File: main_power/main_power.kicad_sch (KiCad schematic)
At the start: 11 parts

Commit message: sync
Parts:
- RV?: value ADDVOLATAGE -> xxxV
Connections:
- net 330DC: now reaches C?.1, C?.1, C?.1, C?.1, D?.3 (+)
- net GND: now reaches C?.2, C?.2, C?.2, C?.2, D?.1 (-)
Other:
- added sheet pico_gate_driver (pico_gate_driver.kicad_sch)
- note added: "230 AC to 330 DC"
- note added: "Amount of capacitors and thier capacity have to be selected manually based on measurements/furnace behaviour and thermal wire resistance."
- note removed: "Amount of capacitors and thier capacity have to be selected manually based on measurements and thermal wire resistance."
- moved on the sheet: C?, D?, F?, P?, RV?

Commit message: repo cleaning
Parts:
- added TP?: BINDIN_POST, symbol Connector:TestPoint
- added TP?: BINDING_POST, symbol Connector:TestPoint
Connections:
- net GND renamed GND1
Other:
- added sheet PICO (pico.kicad_sch)
- added sheet converter (converter.kicad_sch)
- note added: "230 AC to 320 DC"
- note removed: "230 AC to 330 DC"
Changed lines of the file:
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@@
 		)
 	)
-	(text "230 AC to 330 DC"
+	(text "230 AC to 320 DC"
 		(exclude_from_sim no)
 		(at 100.838 17.78 0)
@@
 	)
 	(symbol
+		(lib_id "Connector:TestPoint")
+		(at 198.12 52.07 180)
+		(unit 1)
+		(exclude_from_sim no)
+		(in_bom yes)
+		(on_board yes)
+		(dnp no)
+		(fields_autoplaced yes)
+		(property "Reference" "TP?"
+			(at 200.66 54.1019 0)
+			(effects
+				(font
+					(size 1.27 1.27)
+				)
+				(justify right)
+			)
+		)
+		(property "Value" "BINDIN_POST"
+			(at 200.66 56.6419 0)
+			(effects
+				(font
+					(size 1.27 1.27)
+				)
+				(justify right)
+			)
+		)
+		(property "Footprint" ""
+			(at 193.04 52.07 0)
+			(effects
+				(font
+					(size 1.27 1.27)
+				)
+				(hide yes)
+			)
+		)
+		(property "Datasheet" "~"
+			(at 193.04 52.07 0)
+			(effects
+				(font
+					(size 1.27 1.27)
+				)
+				(hide yes)
+			)
+		)
+		(property "Description" "test point"
+			(at 198.12 52.07 0)
+			(effects
+				(font
+					(size 1.27 1.27)
+				)
+				(hide yes)
+			)
+		)
+		(pin "1"
+		)
+		(instances
+			(project "main_power"
+				(path "/26414091-898c-43ca-a448-286047dacb70"
+					(reference "TP?")
+					(unit 1)
+				)
+			)
+		)
+	)
+	(symbol
 		(lib_id "Connector:Conn_WallPlug_Earth")
 		(at 29.21 39.37 0)
@@
 	)
 	(symbol
+		(lib_id "Connector:TestPoint")
+		(at 196.85 39.37 0)
+		(unit 1)
+		(exclude_from_sim no)
+		(in_bom yes)
+		(on_board yes)
+		(dnp no)
+		(fields_autoplaced yes)
+		(property "Reference" "TP?"
+			(at 199.39 34.7979 0)
+			(effects
+				(font
+					(size 1.27 1.27)
+				)
+				(justify left)
+			)
+		)
+		(property "Value" "BINDING_POST"
+			(at 199.39 37.3379 0)
+			(effects
+				(font
+					(size 1.27 1.27)
+				)
+				(justify left)
+			)
+		)
+		(property "Footprint" ""
+			(at 201.93 39.37 0)
+			(effects
+				(font
+					(size 1.27 1.27)
+				)
+				(hide yes)
+			)
+		)
+		(property "Datasheet" "~"
+			(at 201.93 39.37 0)
+			(effects
+				(font
+					(size 1.27 1.27)
+				)
+				(hide yes)
+			)
+		)
+		(property "Description" "test point"
+			(at 196.85 39.37 0)
+			(effects
+				(font
+					(size 1.27 1.27)
+				)
+				(hide yes)
+			)
+		)
+		(pin "1"
+		)
+		(instances
+			(project "main_power"
+				(path "/26414091-898c-43ca-a448-286047dacb70"
+					(reference "TP?")
+					(unit 1)
+				)
+			)
+		)
+	)
+	(symbol
 		(lib_id "Device:Fuse")
 		(at 73.66 31.75 270)
@@
 	)
 	(symbol
-		(lib_id "power:GND")
+		(lib_id "Device:C_Polarized")
+		(at 125.73 45.72 0)
+		(unit 1)
+		(exclude_from_sim no)
+		(in_bom yes)
+		(on_board yes)
+		(dnp no)
+		(fields_autoplaced yes)
+		(property "Reference" "C?"
+			(at 129.54 43.5609 0)
+			(effects
+				(font
+					(size 1.27 1.27)
+				)
+				(justify left)
+			)
+		)
+		(property "Value" "330u"
+			(at 129.54 46.1009 0)
+			(effects
+				(font
+					(size 1.27 1.27)
+				)
+				(justify left)
+			)
+		)
+		(property "Footprint" ""
+			(at 126.6952 49.53 0)
+			(effects
+				(font
+					(size 1.27 1.27)
+				)
+				(hide yes)
+			)
+		)
+		(property "Datasheet" "~"
+			(at 125.73 45.72 0)
+			(effects
+				(font
+					(size 1.27 1.27)
+				)
+				(hide yes)
+			)
+		)
+		(property "Description" "Polarized capacitor"
+			(at 125.73 45.72 0)
+			(effects
+				(font
+					(size 1.27 1.27)
+				)
+				(hide yes)
+			)
+		)
+		(pin "2"
+		)
+		(pin "1"
+		)
+		(instances
+			(project "main_power"
+				(path "/26414091-898c-43ca-a448-286047dacb70"
+					(reference "C?")
+					(unit 1)
+				)
+			)
+		)
+	)
+	(symbol
+		(lib_id "power:GND1")
 		(at 190.5 52.07 0)
 		(unit 1)
@@
 		(dnp no)
 		(fields_autoplaced yes)
-		(property "Reference" "#PWR01"
+		(property "Reference" "#PWR02"
 			(at 190.5 58.42 0)
 			(effects
@@
 			)
 		)
-		(property "Value" "GND"
+		(property "Value" "GND1"
 			(at 190.5 57.15 0)
 			(effects
@@
 			)
 		)
-		(property "Description" "Power symbol creates a global label with name \"GND\" , ground"
+		(property "Description" "Power symbol creates a global label with name \"GND1\" , ground"
 			(at 190.5 52.07 0)
 			(effects
@@
 			(project "main_power"
 				(path "/26414091-898c-43ca-a448-286047dacb70"
-					(reference "#PWR01")
-					(unit 1)
-				)
-			)
-		)
-	)
-	(symbol
-		(lib_id "Device:C_Polarized")
-		(at 125.73 45.72 0)
-		(unit 1)
-		(exclude_from_sim no)
-		(in_bom yes)
-		(on_board yes)
-		(dnp no)
-		(fields_autoplaced yes)
-		(property "Reference" "C?"
-			(at 129.54 43.5609 0)
-			(effects
-				(font
-					(size 1.27 1.27)
-				)
-				(justify left)
-			)
-		)
-		(property "Value" "330u"
-			(at 129.54 46.1009 0)
-			(effects
-				(font
-					(size 1.27 1.27)
-				)
-				(justify left)
-			)
-		)
-		(property "Footprint" ""
-			(at 126.6952 49.53 0)
-			(effects
-				(font
-					(size 1.27 1.27)
-				)
-				(hide yes)
-			)
-		)
-		(property "Datasheet" "~"
-			(at 125.73 45.72 0)
-			(effects
-				(font
-					(size 1.27 1.27)
-				)
-				(hide yes)
-			)
-		)
-		(property "Description" "Polarized capacitor"
-			(at 125.73 45.72 0)
-			(effects
-				(font
-					(size 1.27 1.27)
-				)
-				(hide yes)
-			)
-		)
-		(pin "2"
-		)
-		(pin "1"
-		)
-		(instances
-			(project "main_power"
-				(path "/26414091-898c-43ca-a448-286047dacb70"
-					(reference "C?")
+					(reference "#PWR02")
 					(unit 1)
 				)
@@
 					(reference "C?")
 					(unit 1)
+				)
+			)
+		)
+	)
+	(sheet
+		(at 38.862 97.028)
+		(size 89.154 24.638)
+		(fields_autoplaced yes)
+		(stroke
+			(width 0.1524)
+			(type solid)
+		)
+		(fill
+			(color 0 0 0 0.0000)
+		)
+		(property "Sheetname" "converter"
+			(at 38.862 96.3164 0)
+			(effects
+				(font
+					(size 1.27 1.27)
+				)
+				(justify left bottom)
+			)
+		)
+		(property "Sheetfile" "converter.kicad_sch"
+			(at 38.862 122.2506 0)
+			(effects
+				(font
+					(size 1.27 1.27)
+				)
+				(justify left top)
+			)
+		)
+		(instances
+			(project "main_power"
+				(path "/26414091-898c-43ca-a448-286047dacb70"
+					(page "4")
 				)
 			)
@@
 				)
 			)
+		)
+	)
+	(sheet
+		(at 183.134 138.684)
+		(size 78.994 21.082)
+		(fields_autoplaced yes)
+		(stroke
+			(width 0.1524)
+			(type solid)
+		)
+		(fill
+			(color 0 0 0 0.0000)
+		)
+		(property "Sheetname" "PICO"
+			(at 183.134 137.9724 0)
+			(effects
+				(font
+					(size 1.27 1.27)
+				)
+				(justify left bottom)
+			)
+		)
+		(property "Sheetfile" "pico.kicad_sch"
+			(at 183.134 160.3506 0)
+			(effects
+				(font
+					(size 1.27 1.27)
+				)
+				(justify left top)
+			)
+		)
+		(instances
+			(project "main_power"
+				(path "/26414091-898c-43ca-a448-286047dacb70"
+					(page "3")
+				)
+			)

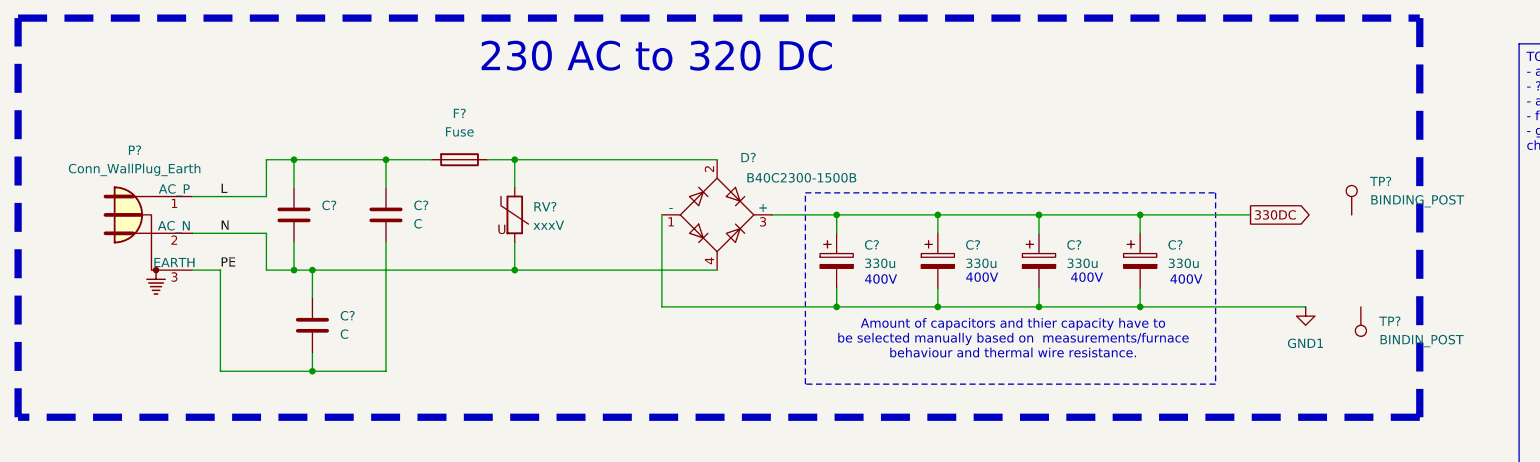
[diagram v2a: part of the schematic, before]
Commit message: schematic of flyback v1
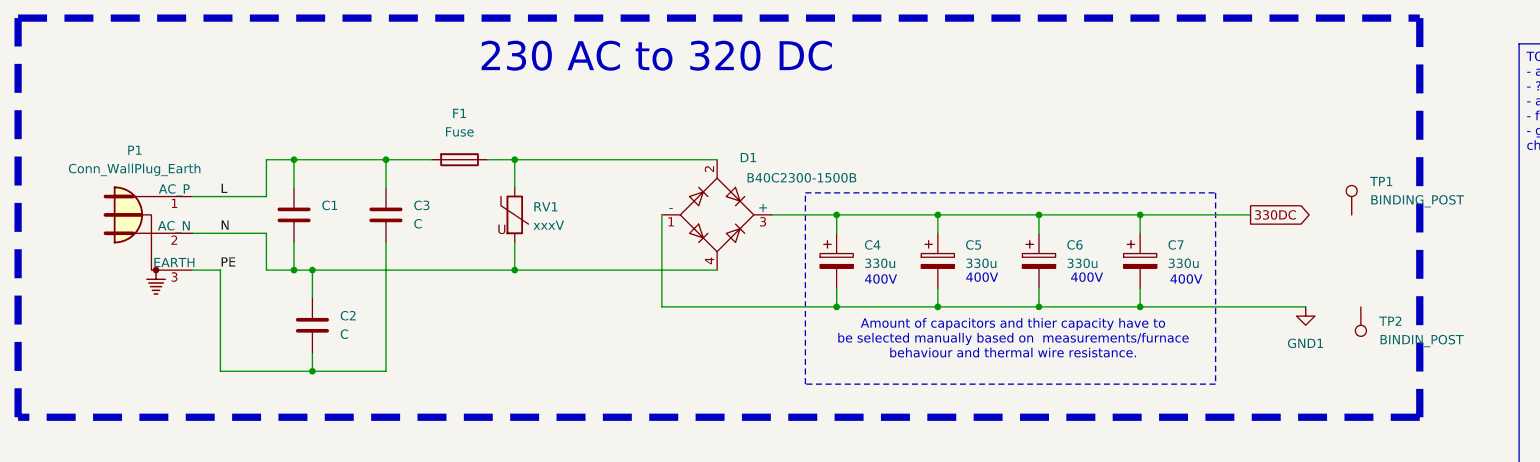
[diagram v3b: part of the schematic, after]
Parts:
- gave numbers to parts that had none: 13
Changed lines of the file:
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@@
 		(dnp no)
 		(fields_autoplaced yes)
-		(property "Reference" "TP?"
+		(property "Reference" "TP2"
 			(at 200.66 54.1019 0)
 			(effects
@@
 			(project "main_power"
 				(path "/26414091-898c-43ca-a448-286047dacb70"
-					(reference "TP?")
+					(reference "TP2")
 					(unit 1)
 				)
@@
 		(dnp no)
 		(fields_autoplaced yes)
-		(property "Reference" "P?"
+		(property "Reference" "P1"
 			(at 28.8163 30.48 0)
 			(effects
@@
 			(project "main_power"
 				(path "/26414091-898c-43ca-a448-286047dacb70"
-					(reference "P?")
+					(reference "P1")
 					(unit 1)
 				)
@@
 		(dnp no)
 		(fields_autoplaced yes)
-		(property "Reference" "C?"
+		(property "Reference" "C6"
 			(at 157.48 43.5609 0)
 			(effects
@@
 			(project "main_power"
 				(path "/26414091-898c-43ca-a448-286047dacb70"
-					(reference "C?")
+					(reference "C6")
 					(unit 1)
 				)
@@
 		(dnp no)
 		(fields_autoplaced yes)
-		(property "Reference" "RV?"
+		(property "Reference" "RV1"
 			(at 83.82 38.2932 0)
 			(effects
@@
 			(project "main_power"
 				(path "/26414091-898c-43ca-a448-286047dacb70"
-					(reference "RV?")
+					(reference "RV1")
 					(unit 1)
 				)
@@
 		(on_board yes)
 		(dnp no)
-		(property "Reference" "D?"
+		(property "Reference" "D1"
 			(at 113.538 31.496 0)
 			(effects
@@
 			(project "main_power"
 				(path "/26414091-898c-43ca-a448-286047dacb70"
-					(reference "D?")
+					(reference "D1")
 					(unit 1)
 				)
@@
 		(dnp no)
 		(fields_autoplaced yes)
-		(property "Reference" "C?"
+		(property "Reference" "C1"
 			(at 54.61 38.0999 0)
 			(effects
@@
 			(project "main_power"
 				(path "/26414091-898c-43ca-a448-286047dacb70"
-					(reference "C?")
+					(reference "C1")
 					(unit 1)
 				)
@@
 		(dnp no)
 		(fields_autoplaced yes)
-		(property "Reference" "C?"
+		(property "Reference" "C3"
 			(at 67.31 38.0999 0)
 			(effects
@@
 			(project "main_power"
 				(path "/26414091-898c-43ca-a448-286047dacb70"
-					(reference "C?")
+					(reference "C3")
 					(unit 1)
 				)
@@
 		(dnp no)
 		(fields_autoplaced yes)
-		(property "Reference" "C?"
+		(property "Reference" "C2"
 			(at 57.15 53.3399 0)
 			(effects
@@
 			(project "main_power"
 				(path "/26414091-898c-43ca-a448-286047dacb70"
-					(reference "C?")
+					(reference "C2")
 					(unit 1)
 				)
@@
 		(dnp no)
 		(fields_autoplaced yes)
-		(property "Reference" "TP?"
+		(property "Reference" "TP1"
 			(at 199.39 34.7979 0)
 			(effects
@@
 			(project "main_power"
 				(path "/26414091-898c-43ca-a448-286047dacb70"
-					(reference "TP?")
+					(reference "TP1")
 					(unit 1)
 				)
@@
 		(dnp no)
 		(fields_autoplaced yes)
-		(property "Reference" "F?"
+		(property "Reference" "F1"
 			(at 73.66 25.4 90)
 			(effects
@@
 			(project "main_power"
 				(path "/26414091-898c-43ca-a448-286047dacb70"
-					(reference "F?")
+					(reference "F1")
 					(unit 1)
 				)
@@
 		(dnp no)
 		(fields_autoplaced yes)
-		(property "Reference" "C?"
+		(property "Reference" "C7"
 			(at 171.45 43.5609 0)
 			(effects
@@
 			(project "main_power"
 				(path "/26414091-898c-43ca-a448-286047dacb70"
-					(reference "C?")
+					(reference "C7")
 					(unit 1)
 				)
@@
 		(dnp no)
 		(fields_autoplaced yes)
-		(property "Reference" "C?"
+		(property "Reference" "C4"
 			(at 129.54 43.5609 0)
 			(effects
@@
 			(project "main_power"
 				(path "/26414091-898c-43ca-a448-286047dacb70"
-					(reference "C?")
+					(reference "C4")
 					(unit 1)
 				)
@@
 		(dnp no)
 		(fields_autoplaced yes)
-		(property "Reference" "C?"
+		(property "Reference" "C5"
 			(at 143.51 43.5609 0)
 			(effects
@@
 			(project "main_power"
 				(path "/26414091-898c-43ca-a448-286047dacb70"
-					(reference "C?")
-					(unit 1)
-				)
+					(reference "C5")
+					(unit 1)
+				)
